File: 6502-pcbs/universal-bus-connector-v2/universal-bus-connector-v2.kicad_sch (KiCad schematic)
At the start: 5 parts, among them J1 Universal Bus Connector v2, J2 Universal Bus Connector v2, J3 Universal Bus Connector v2, J4 Universal Bus Connector v2

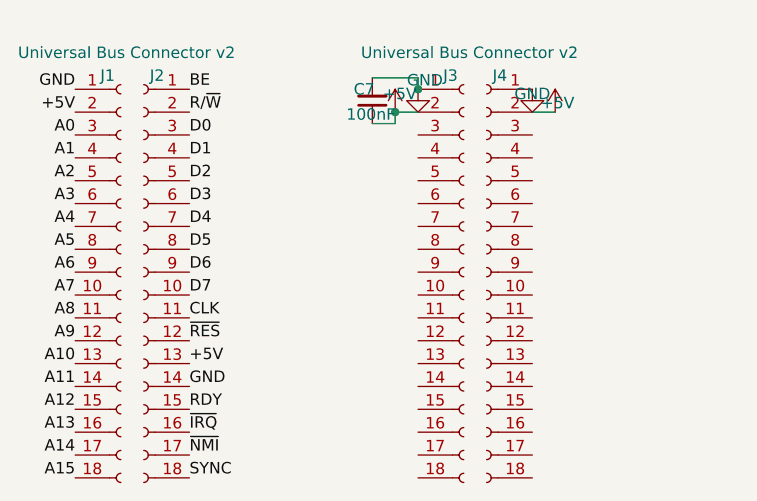
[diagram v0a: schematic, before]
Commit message: 6502 mainboard
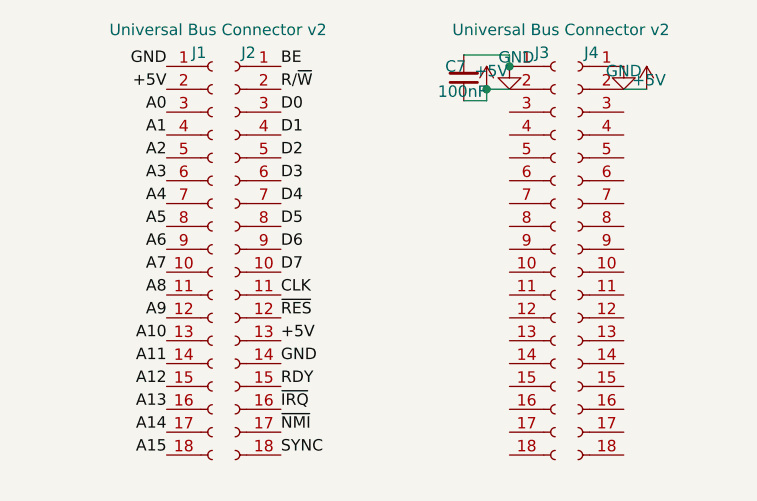
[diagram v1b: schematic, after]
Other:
- company: Sam Warr -> (none)
- title: Universal Bus Connector -> (none)
